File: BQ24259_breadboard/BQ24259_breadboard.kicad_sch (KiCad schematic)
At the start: 24 parts, among them J1 USB_C_Receptacle_USB2.0, J2 Power_In, J3 Battery, J4 PWR_Left, J5 PWR_Right, J6 BatTemp, U1 BQ24259RGER

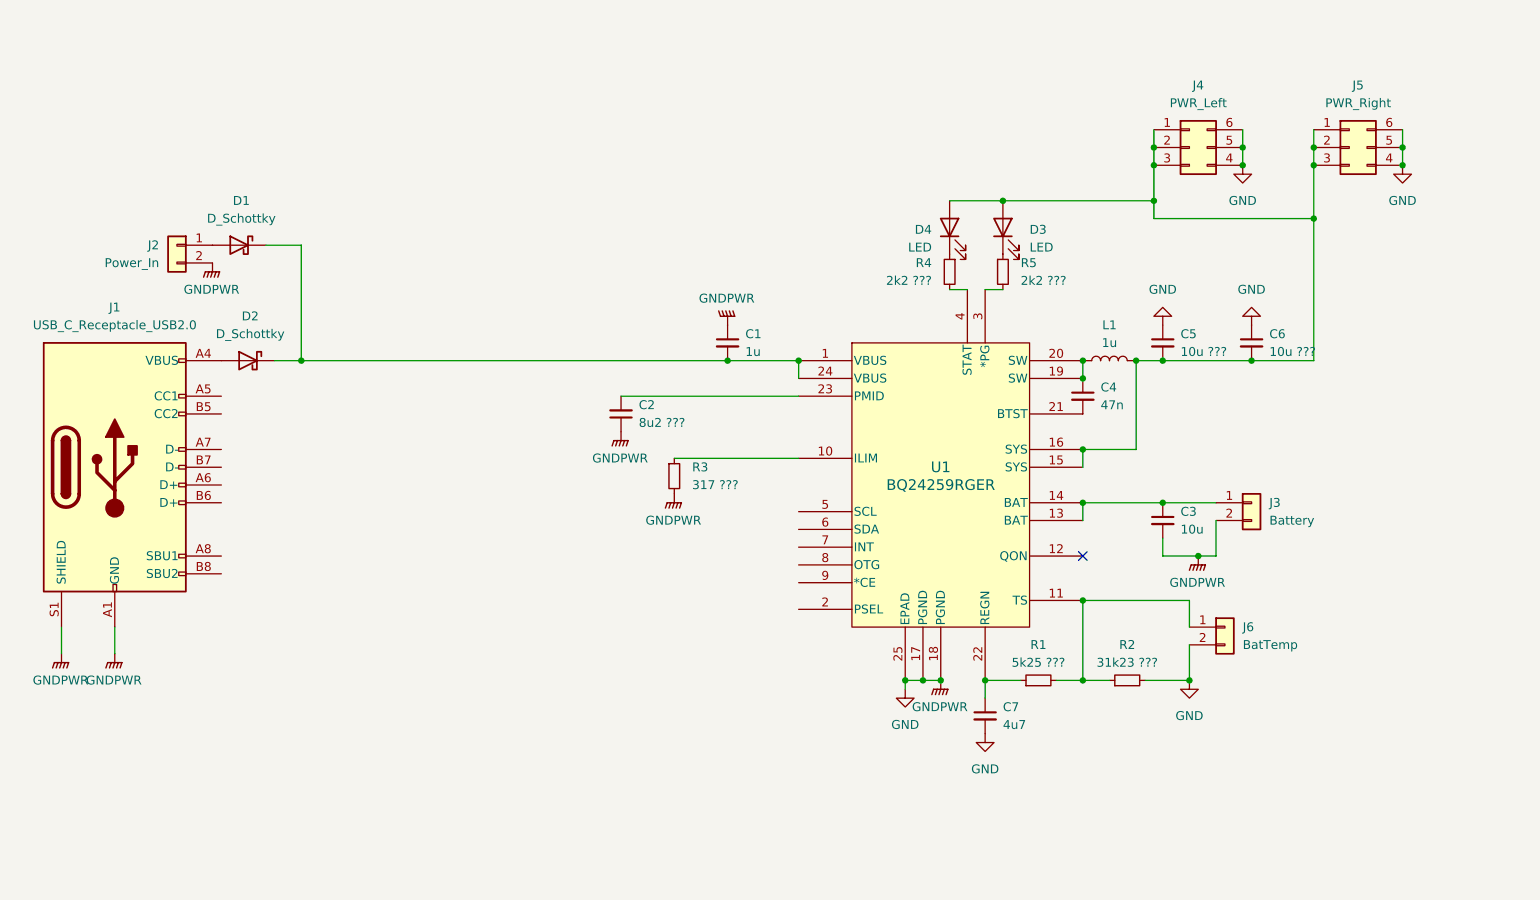
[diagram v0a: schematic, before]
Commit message: Schematic drawing for breadboard power module using BQ24259
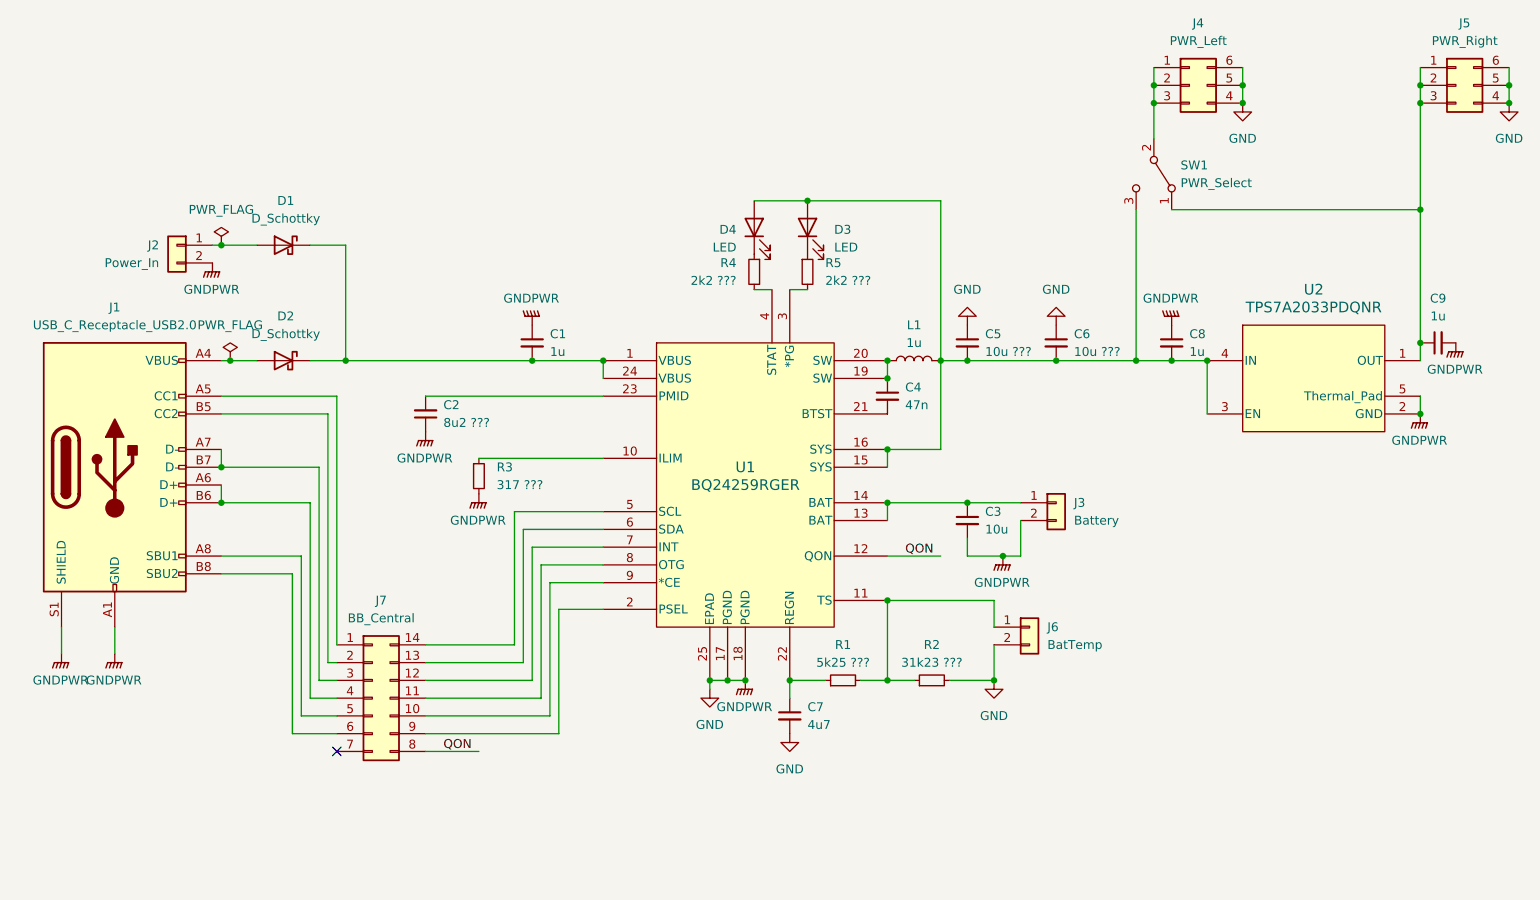
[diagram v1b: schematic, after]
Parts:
- added C8, C9: 1u, symbol Device:C_Small
- added J7: BB_Central, symbol Connector_Generic:Conn_02x07_Counter_Clockwise
- added SW1: PWR_Select, symbol Switch:SW_SPDT
- added U2: TPS7A2033PDQNR, DQN0004A-MFG, symbol Project_Components:TPS7A20
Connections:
- net GND: now also C8.1, C9.2, U2.2 (GND), U2.5 (Thermal_Pad)
- net at C5.2, C6.2, D3.2 (A)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: now also C8.2, SW1.3 (C), U2.3 (EN), U2.4 (IN); no longer J4.1 (Pin_1), J4.2 (Pin_2), J4.3 (Pin_3), J5.1 (Pin_1), J5.2 (Pin_2), J5.3 (Pin_3)
- net at J1.A5 (CC1): now also J7.1 (Pin_1)
- net at J1.A6 (D+): now also J1.B6 (D+), J7.4 (Pin_4)
- net at J1.A7 (D-): now also J1.B7 (D-), J7.3 (Pin_3)
- net at J1.A8 (SBU1): now also J7.5 (Pin_5)
- net at J1.B5 (CC2): now also J7.2 (Pin_2)
- net at J1.B8 (SBU2): now also J7.6 (Pin_6)
- net QON: now reaches U1.12 (QON)
- net QON: now also J7.8 (Pin_8)
- net at U1.2 (PSEL): now also J7.9 (Pin_9)
- net at U1.5 (SCL): now also J7.14 (Pin_14)
- net at U1.6 (SDA): now also J7.13 (Pin_13)
- net at U1.7 (INT): now also J7.12 (Pin_12)
- net at U1.8 (OTG): now also J7.11 (Pin_11)
- net at U1.9 (*CE): now also J7.10 (Pin_10)
- new net: C9.1, J5.1 (Pin_1), J5.2 (Pin_2), J5.3 (Pin_3), SW1.1 (A), U2.1 (OUT)
- new net: J4.1 (Pin_1), J4.2 (Pin_2), J4.3 (Pin_3), SW1.2 (B)
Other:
- moved on the sheet: C1, C2, C3, C4, C5, C6, C7, D1, D2, D3, D4, J3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

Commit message: Fix small issues in schema
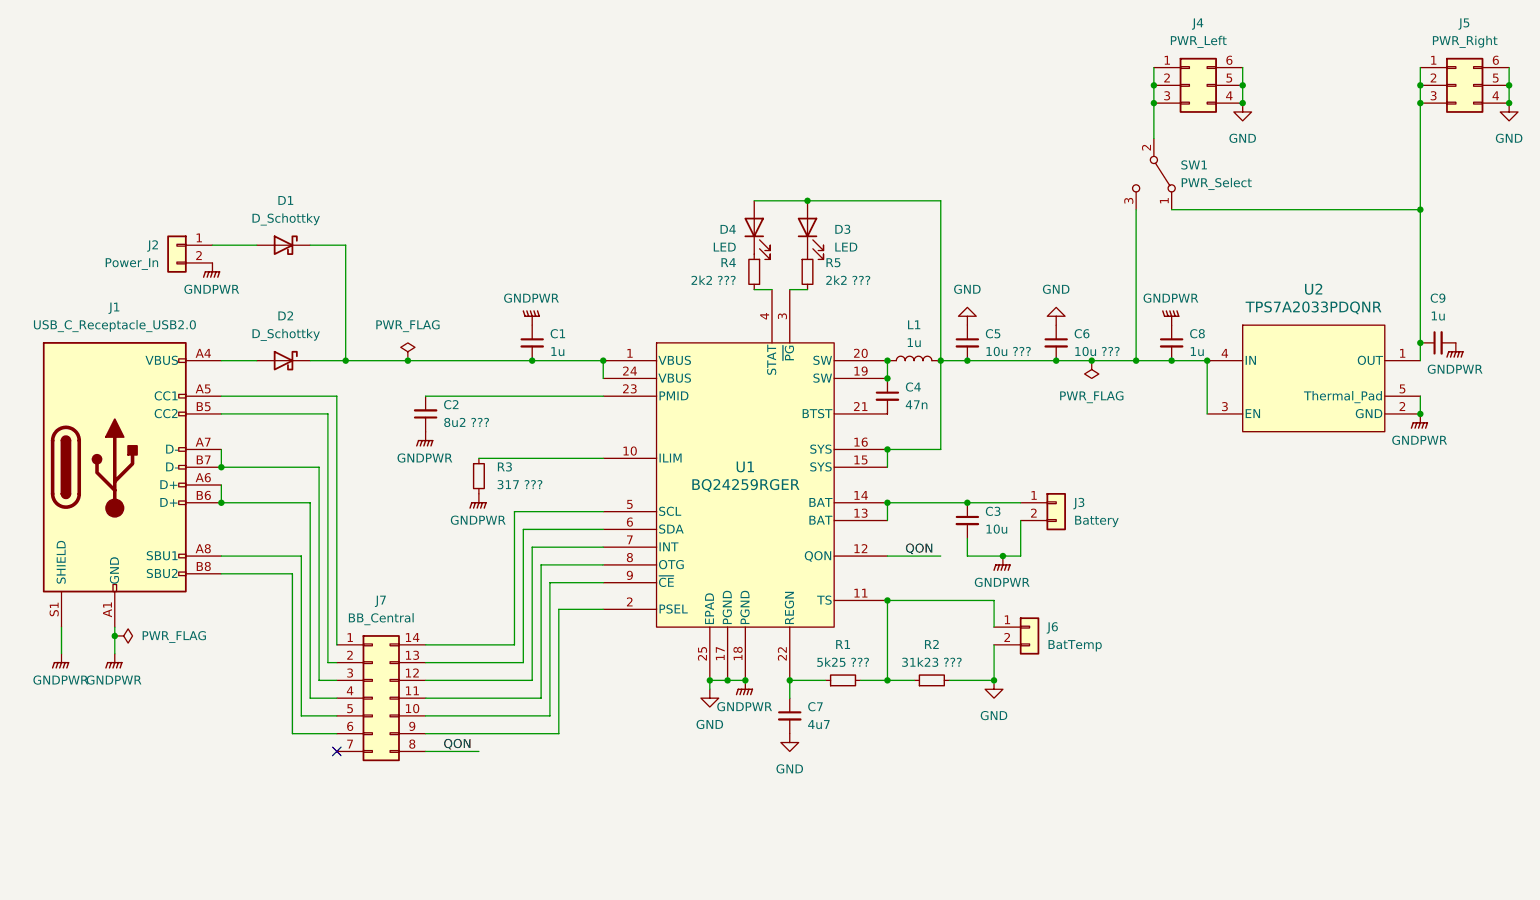
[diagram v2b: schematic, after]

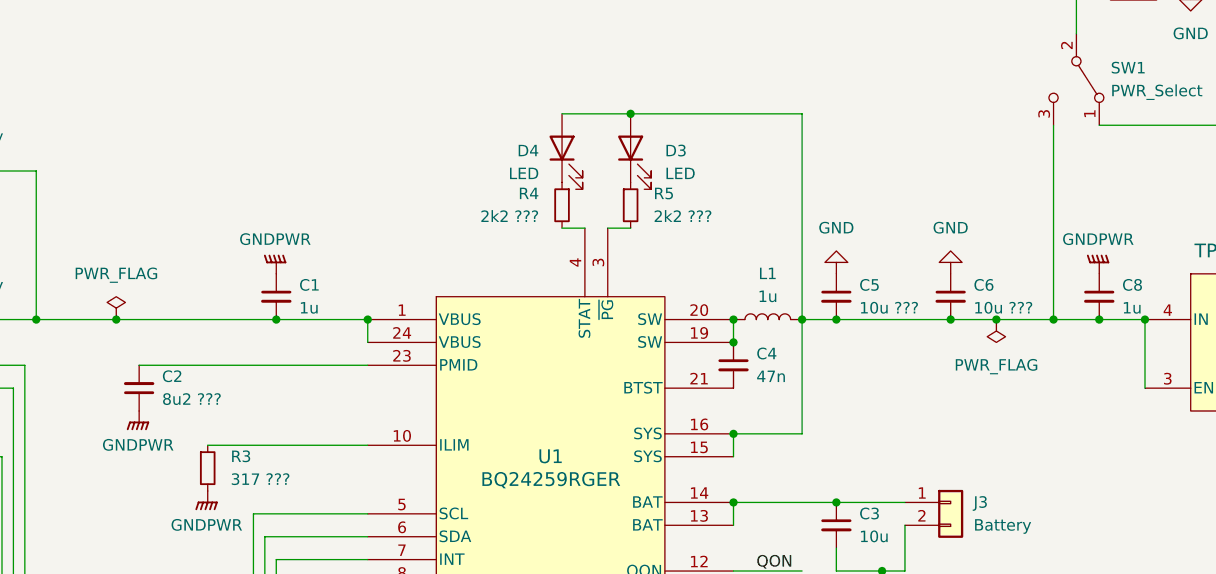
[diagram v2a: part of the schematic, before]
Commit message: Partially assigned footprints
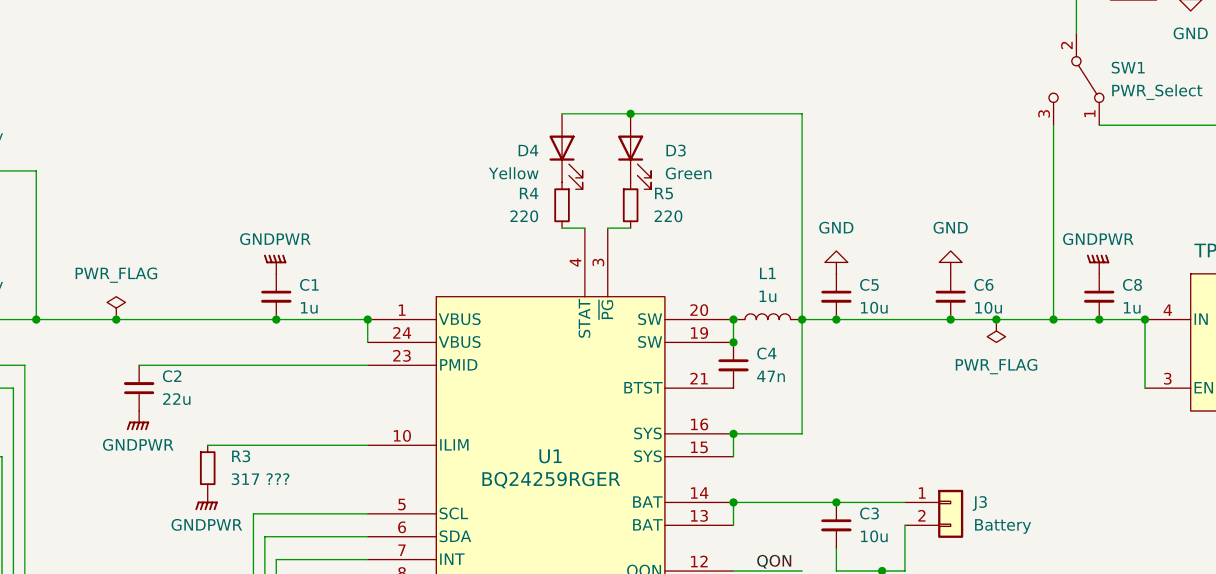
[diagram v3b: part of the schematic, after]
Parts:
- C1: footprint (none) -> Connector_JST:JST_PH_B2B-PH-SM4-TB_1x02-1MP_P2.00mm_Vertical; JLCPCB PN (none) -> C15849
- C2: value 8u2 ??? -> 22u; footprint (none) -> Capacitor_SMD:C_0805_2012Metric; JLCPCB PN (none) -> C45783
- C3: footprint (none) -> Capacitor_SMD:C_0603_1608Metric; JLCPCB PN (none) -> C19702
- C4: footprint (none) -> Capacitor_SMD:C_0603_1608Metric; JLCPCB PN (none) -> C1622
- C5, C6: value 10u ??? -> 10u; footprint (none) -> Capacitor_SMD:C_0603_1608Metric; JLCPCB PN (none) -> C19702
- C7: footprint (none) -> Capacitor_SMD:C_0402_1005Metric; JLCPCB PN (none) -> C23733
- C8, C9: footprint (none) -> Capacitor_SMD:C_0402_1005Metric; JLCPCB PN (none) -> C52923
- D1, D2: footprint (none) -> Diode_SMD:D_SMA; JLCPCB PN (none) -> C8678
- D3: value LED -> Green; footprint (none) -> LED_SMD:LED_0603_1608Metric; JLCPCB PN (none) -> C72043
- D4: value LED -> Yellow; footprint (none) -> LED_SMD:LED_0603_1608Metric; JLCPCB PN (none) -> C72038
- J1: footprint (none) -> Project_Footprints:USB4105_GCT
- J2: footprint (none) -> Connector_PinHeader_2.54mm:PinHeader_1x02_P2.54mm_Vertical
- J3, J6: footprint (none) -> Connector_JST:JST_PH_B2B-PH-SM4-TB_1x02-1MP_P2.00mm_Vertical
- J4, J5: footprint (none) -> Connector_PinHeader_2.54mm:PinHeader_2x03_P2.54mm_Vertical
- L1: footprint (none) -> Inductor_SMD:L_Murata_DFE201610P
- R4, R5: value 2k2 ??? -> 220; footprint (none) -> Resistor_SMD:R_0603_1608Metric; JLCPCB PN (none) -> C22962
- SW1: footprint (none) -> Connector_PinHeader_2.54mm:PinHeader_1x03_P2.54mm_Vertical
- U1: footprint RGE24_2P7X2P7_TEX -> Project_Footprints:RGE24_2P7X2P7_TEX
- U2: footprint DQN0004A-MFG -> Project_Footprints:DQN0004A-MFG

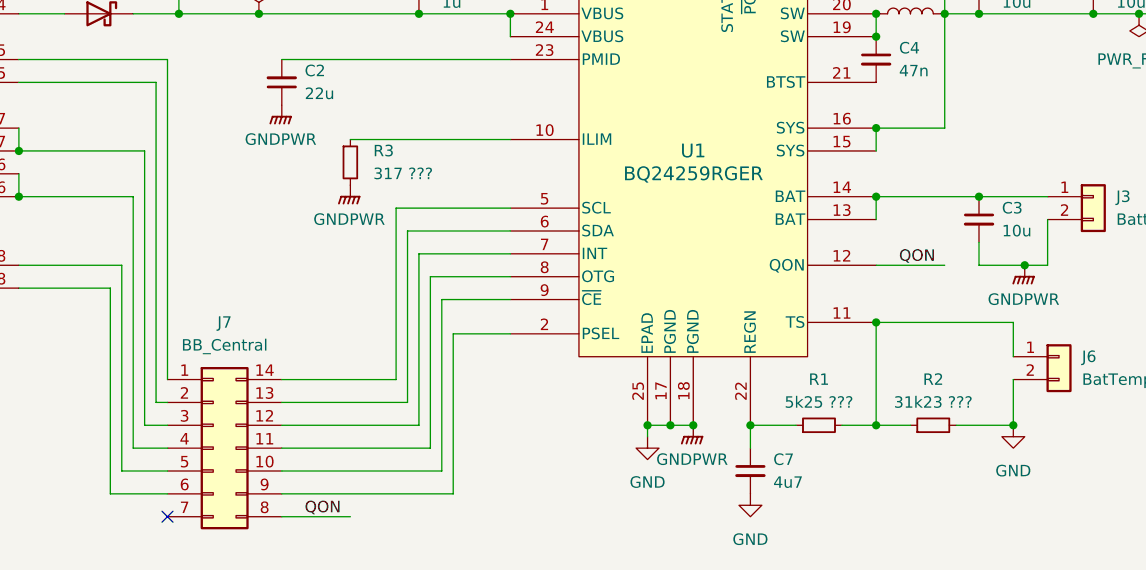
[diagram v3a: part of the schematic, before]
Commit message: Power board with all components assigned
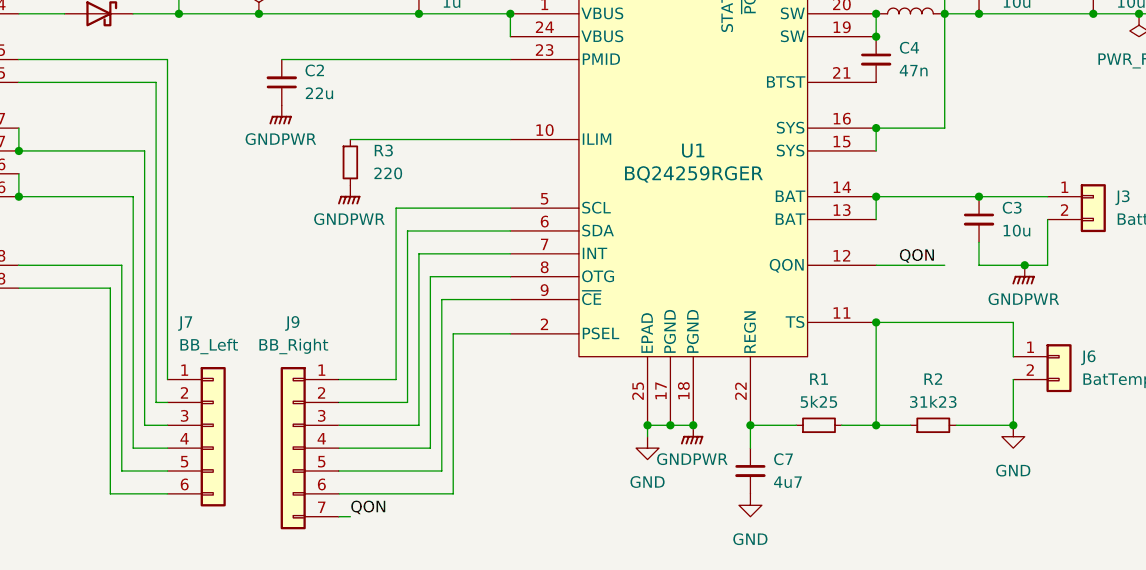
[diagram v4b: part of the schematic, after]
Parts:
- removed J7: BB_Central, symbol Connector_Generic:Conn_02x07_Counter_Clockwise
- added J7: BB_Left, Connector_PinHeader_2.54mm:PinHeader_1x06_P2.54mm_Vertical, symbol Connector_Generic:Conn_01x06
- added J9: BB_Right, Connector_PinHeader_2.54mm:PinHeader_1x07_P2.54mm_Vertical, symbol Connector_Generic:Conn_01x07
- R1: value 5k25 ??? -> 5k25; footprint (none) -> Resistor_SMD:R_0402_1005Metric
- R2: value 31k23 ??? -> 31k23; footprint (none) -> Resistor_SMD:R_0402_1005Metric
- R3: value 317 ??? -> 220; footprint (none) -> Resistor_SMD:R_0402_1005Metric; JLCPCB PN (none) -> C25091
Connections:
- net QON: now also J9.7 (Pin_7)
- net at J1.A5 (CC1): now also J7.1 (Pin_1)
- net at J1.A6 (D+), J1.B6 (D+): now also J7.4 (Pin_4)
- net at J1.A7 (D-), J1.B7 (D-): now also J7.3 (Pin_3)
- net at J1.A8 (SBU1): now also J7.5 (Pin_5)
- net at J1.B5 (CC2): now also J7.2 (Pin_2)
- net at J1.B8 (SBU2): now also J7.6 (Pin_6)
- net at U1.2 (PSEL): now also J9.6 (Pin_6)
- net at U1.5 (SCL): now also J9.1 (Pin_1)
- net at U1.6 (SDA): now also J9.2 (Pin_2)
- net at U1.7 (INT): now also J9.3 (Pin_3)
- net at U1.8 (OTG): now also J9.4 (Pin_4)
- net at U1.9 (~{CE}): now also J9.5 (Pin_5)
- no-connect marks 1 -> 0
